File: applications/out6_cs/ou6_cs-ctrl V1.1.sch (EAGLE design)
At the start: 82 parts, among them P3 SE1.5, P4 SE1.5, P5 SE1.5, Q1 BCP52, T1 AX1500, T2 AX1500, T3 AX1500, T4 AX1500, T5 AX1500, T6 AX1500, U1 74LV4051D, U2 OPA365AIDBV, U3 OPA365AIDBV, U4 OPA365AIDBV

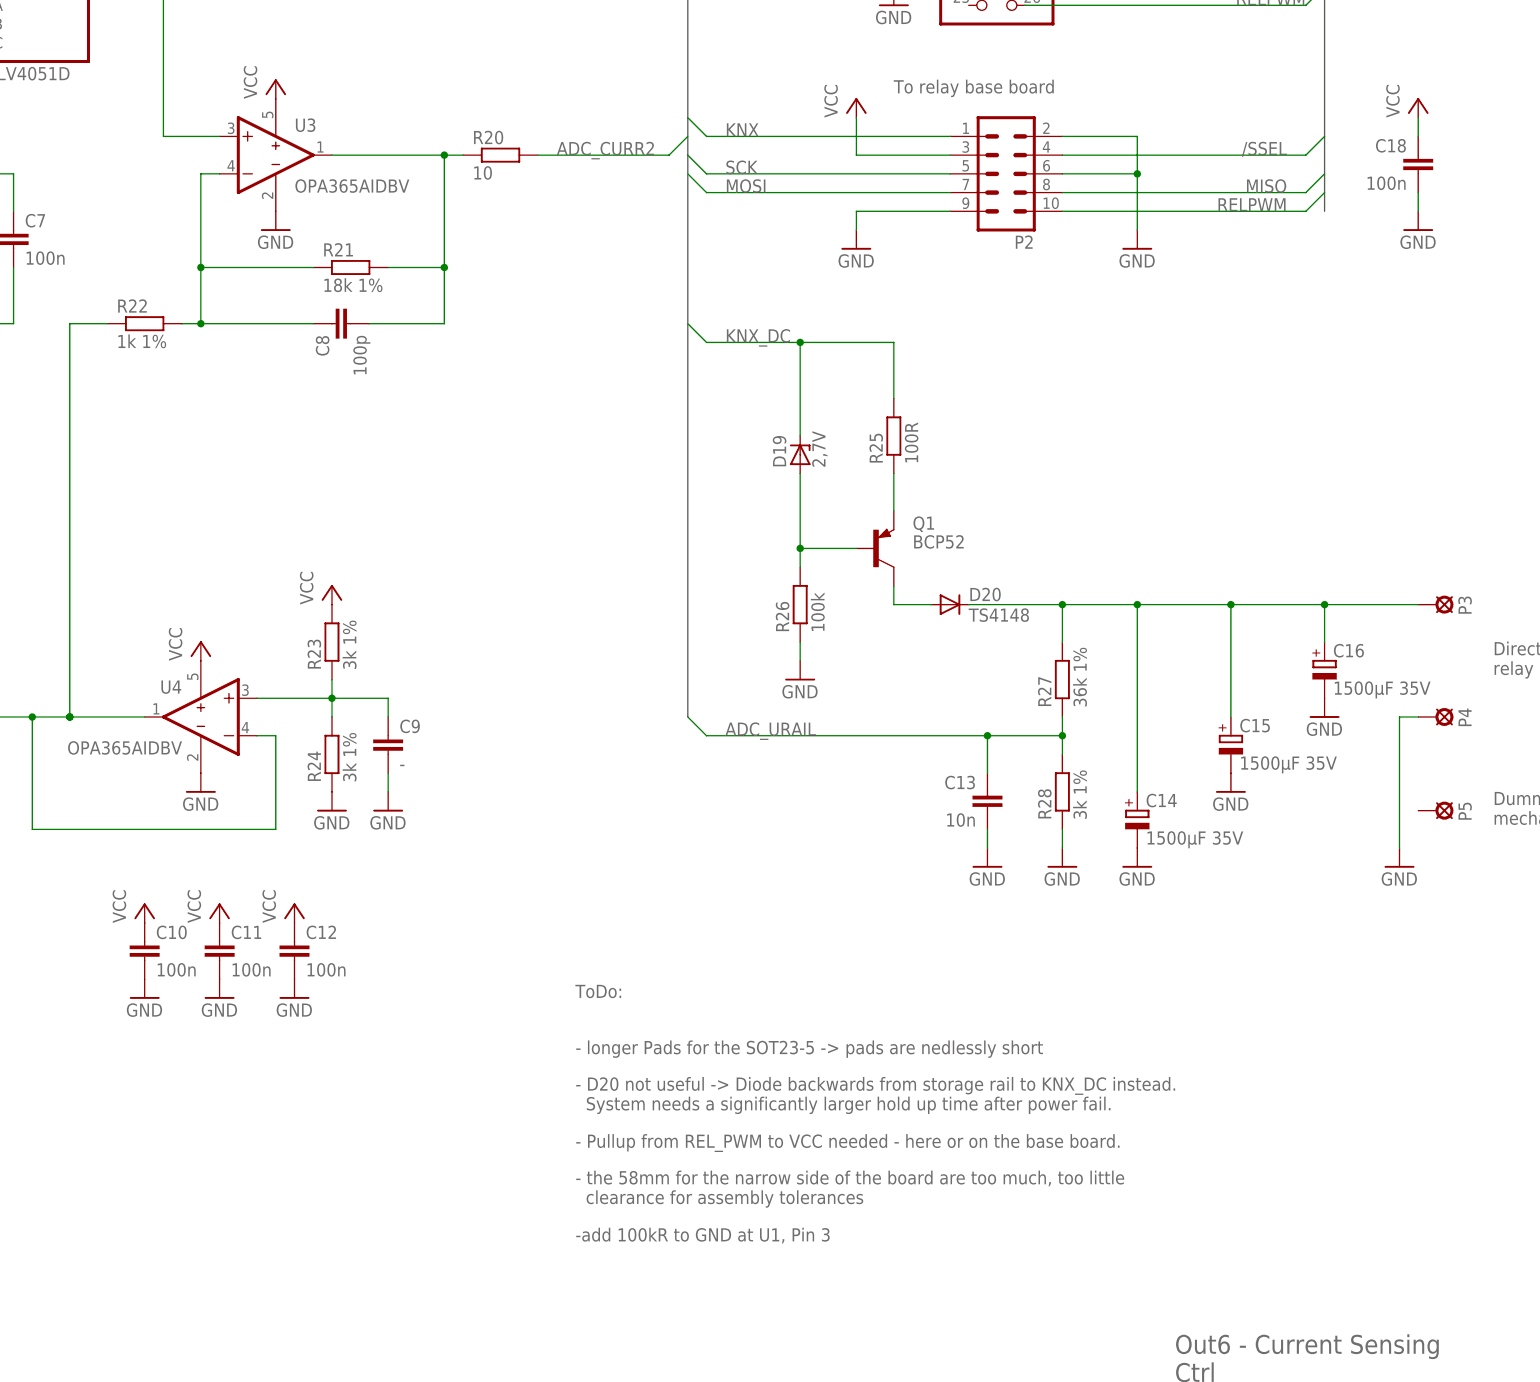
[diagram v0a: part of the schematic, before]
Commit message: Update App out6_cs, update Controller lpc1115_4te_top
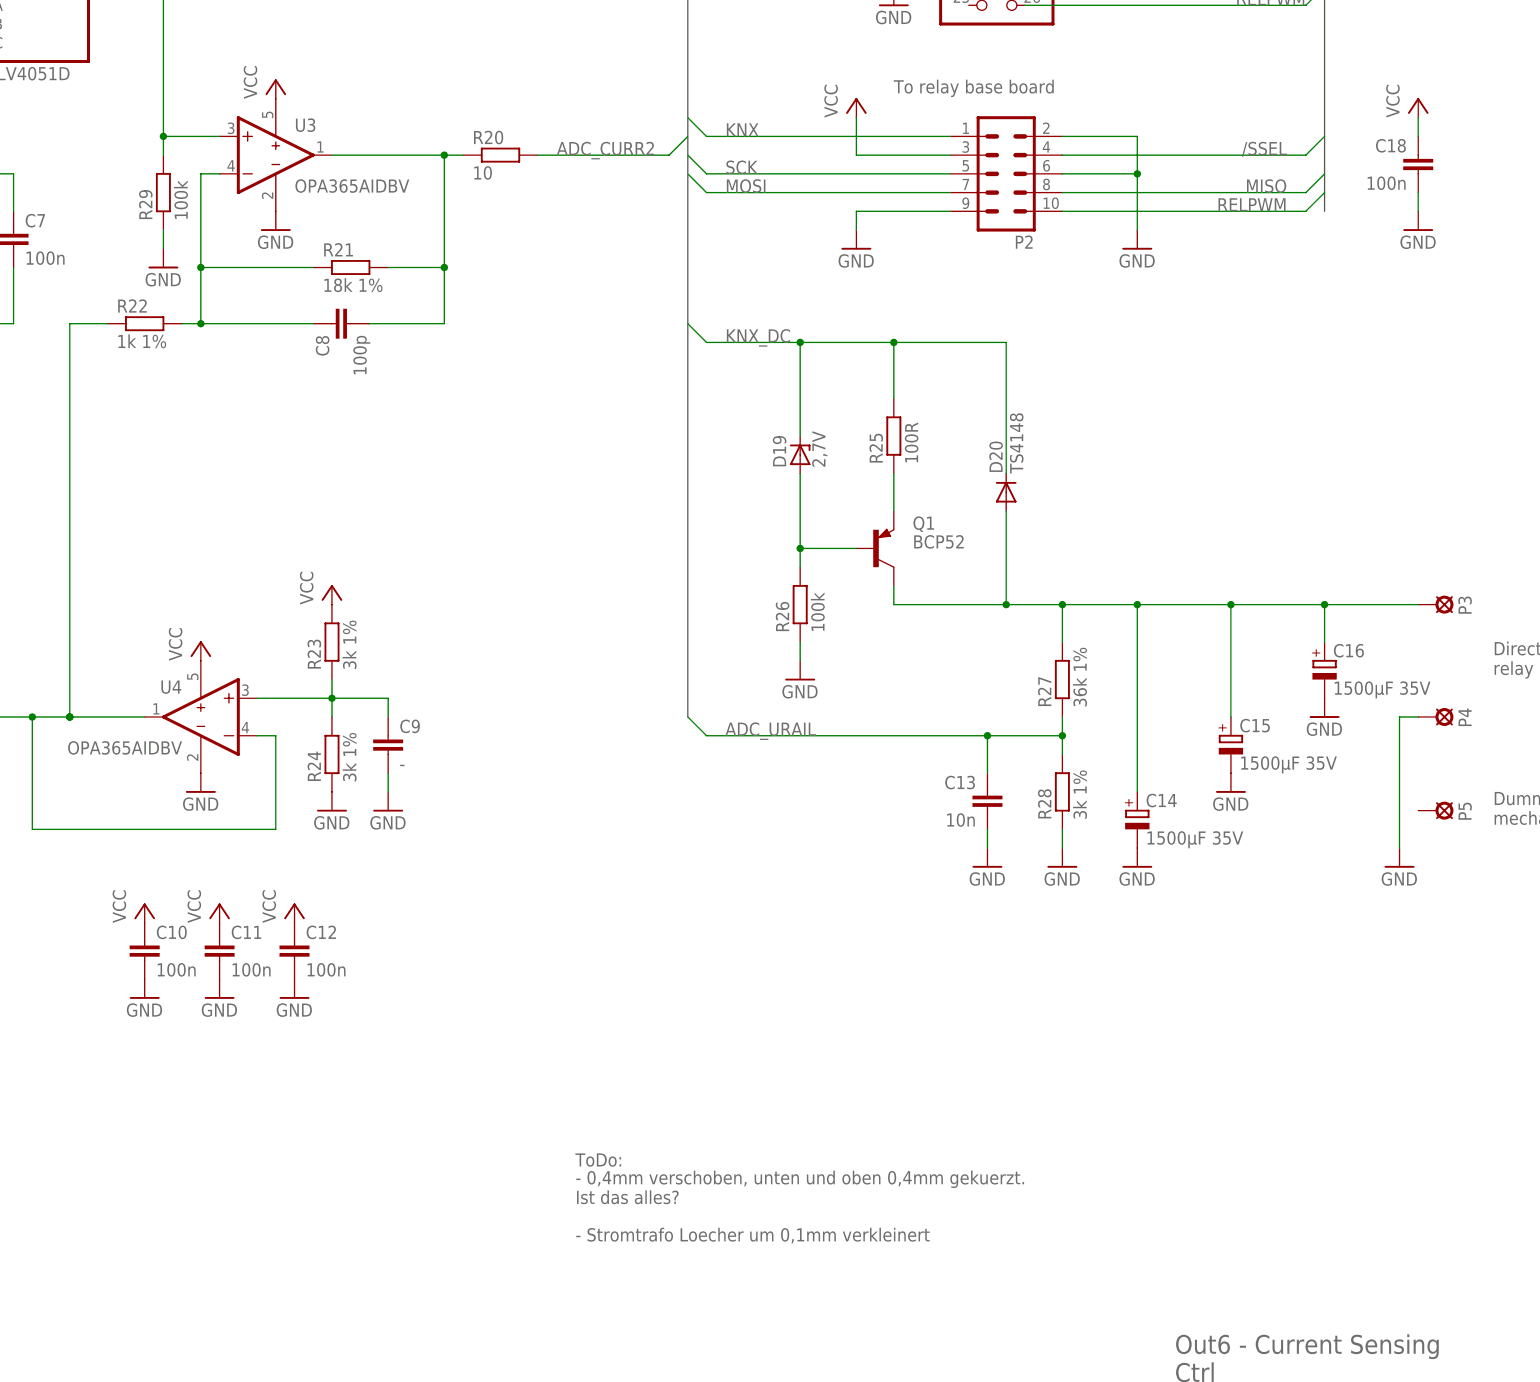
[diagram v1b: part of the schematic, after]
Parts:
- added R29: 100k, rcl:R-EU_R0805M
- D20: device diode:DIODE-MINIMELF -> diode:DIODE-D0805
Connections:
- removed net N$39: C14.+, C15.+, C16.+, D20.C, P3.MP, R27.2
- net GND: now also R29.1
- net KNX_DC: now also D20.C
- net N$16: now also R29.2
- net N$38: now also C14.+, C15.+, C16.+, P3.MP, R27.2
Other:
- note added: "- 0,4mm verschoben, unten und oben 0,4mm gekuerzt. Ist das alles?"
- note added: "- Stromtrafo Loecher um 0,1mm verkleinert"
- note removed: "- D20 not useful -> Diode backwards from storage rail to KNX_DC instead. System needs a significantly larger hold up time after power fail."
- note removed: "- Pullup from REL_PWM to VCC needed - here or on the base board."
- note removed: "- longer Pads for the SOT23-5 -> pads are nedlessly short"
- note removed: "- the 58mm for the narrow side of the board are too much, too little clearance for assembly tolerances"
- note removed: "-add 100kR to GND at U1, Pin 3"
- moved on the sheet: D20
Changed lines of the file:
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@@
 <part name="R26" library="rcl" deviceset="R-EU_" device="R0805M" value="100k"/>
 <part name="D19" library="diode" deviceset="ZENER-DIODE" device="SOT23" value="2,7V"/>
-<part name="D20" library="diode" deviceset="DIODE-" device="MINIMELF" value="TS4148"/>
+<part name="D20" library="diode" deviceset="DIODE-" device="D0805" value="TS4148"/>
 <part name="R27" library="rcl" deviceset="R-EU_" device="R0805M" value="36k 1%"/>
 <part name="R28" library="rcl" deviceset="R-EU_" device="R0805M" value="3k 1%"/>
@@
 <part name="P+11" library="supply1" deviceset="VCC" device=""/>
 <part name="P+12" library="supply1" deviceset="VCC" device=""/>
+<part name="R29" library="rcl" deviceset="R-EU_" device="R0805M" value="100k"/>
+<part name="GND24" library="supply1" deviceset="GND" device=""/>
 </parts>
 <sheets>
@@
 <text x="335.28" y="93.98" size="1.778" layer="95" align="top-left">Dummy connection only as
 mechanical support.</text>
-<text x="210.82" y="66.04" size="1.778" layer="95">ToDo:</text>
-<text x="210.82" y="58.42" size="1.778" layer="95">- longer Pads for the SOT23-5 -&gt; pads are nedlessly short</text>
-<text x="210.82" y="50.8" size="1.778" layer="95">- D20 not useful -&gt; Diode backwards from storage rail to KNX_DC instead.
-  System needs a significantly larger hold up time after power fail.</text>
-<text x="210.82" y="45.72" size="1.778" layer="95">- Pullup from REL_PWM to VCC needed - here or on the base board.</text>
-<text x="210.82" y="38.1" size="1.778" layer="95">- the 58mm for the narrow side of the board are too much, too little
-  clearance for assembly tolerances</text>
-<text x="210.82" y="33.02" size="1.778" layer="95">-add 100kR to GND at U1, Pin 3</text>
+<text x="210.82" y="43.18" size="1.778" layer="95">ToDo:</text>
+<text x="210.82" y="38.1" size="1.778" layer="95">- 0,4mm verschoben, unten und oben 0,4mm gekuerzt.
+Ist das alles?</text>
+<text x="210.82" y="33.02" size="1.778" layer="95">- Stromtrafo Loecher um 0,1mm verkleinert</text>
 </plain>
 <instances>
@@
 <instance part="R26" gate="G$1" x="241.3" y="119.38" rot="R90"/>
 <instance part="D19" gate="G$1" x="241.3" y="139.7" rot="R90"/>
-<instance part="D20" gate="G$1" x="261.62" y="119.38"/>
+<instance part="D20" gate="G$1" x="269.24" y="134.62" rot="R90"/>
 <instance part="R27" gate="G$1" x="276.86" y="109.22" rot="R90"/>
 <instance part="R28" gate="G$1" x="276.86" y="93.98" rot="R90"/>
@@
 <instance part="P+11" gate="VCC" x="325.12" y="187.96"/>
 <instance part="P+12" gate="VCC" x="325.12" y="226.06"/>
+<instance part="R29" gate="G$1" x="154.94" y="175.26" rot="R90"/>
+<instance part="GND24" gate="1" x="154.94" y="165.1"/>
 </instances>
 <busses>
@@
 <pinref part="GND23" gate="1" pin="GND"/>
 <wire x1="325.12" y1="210.82" x2="325.12" y2="213.36" width="0.1524" layer="91"/>
+</segment>
+<segment>
+<pinref part="R29" gate="G$1" pin="1"/>
+<pinref part="GND24" gate="1" pin="GND"/>
+<wire x1="154.94" y1="170.18" x2="154.94" y2="167.64" width="0.1524" layer="91"/>
 </segment>
 </net>
@@
 <wire x1="154.94" y1="226.06" x2="162.56" y2="226.06" width="0.1524" layer="91"/>
 <junction x="154.94" y="226.06"/>
+<pinref part="R29" gate="G$1" pin="2"/>
+<wire x1="154.94" y1="180.34" x2="154.94" y2="182.88" width="0.1524" layer="91"/>
+<junction x="154.94" y="182.88"/>
 </segment>
 </net>
@@
 <junction x="241.3" y="154.94"/>
 <label x="231.14" y="154.94" size="1.778" layer="95"/>
+<pinref part="D20" gate="G$1" pin="C"/>
+<wire x1="254" y1="154.94" x2="269.24" y2="154.94" width="0.1524" layer="91"/>
+<wire x1="269.24" y1="154.94" x2="269.24" y2="137.16" width="0.1524" layer="91"/>
+<junction x="254" y="154.94"/>
 </segment>
 </net>
@@
 <pinref part="Q1" gate="G$1" pin="C"/>
 <wire x1="254" y1="121.92" x2="254" y2="119.38" width="0.1524" layer="91"/>
-<pinref part="D20" gate="G$1" pin="A"/>
-<wire x1="254" y1="119.38" x2="259.08" y2="119.38" width="0.1524" layer="91"/>
-</segment>
-</net>
-<net name="N$39" class="0">
-<segment>
-<pinref part="D20" gate="G$1" pin="C"/>
-<wire x1="264.16" y1="119.38" x2="276.86" y2="119.38" width="0.1524" layer="91"/>
 <pinref part="R27" gate="G$1" pin="2"/>
 <wire x1="276.86" y1="119.38" x2="276.86" y2="114.3" width="0.1524" layer="91"/>
 <wire x1="276.86" y1="119.38" x2="287.02" y2="119.38" width="0.1524" layer="91"/>
-<junction x="276.86" y="119.38"/>
 <pinref part="P3" gate="1" pin="MP"/>
 <pinref part="C14" gate="G$1" pin="+"/>
@@
 <wire x1="312.42" y1="114.3" x2="312.42" y2="119.38" width="0.1524" layer="91"/>
 <junction x="312.42" y="119.38"/>
-</segment>
-</net>
+<wire x1="254" y1="119.38" x2="269.24" y2="119.38" width="0.1524" layer="91"/>
+<junction x="276.86" y="119.38"/>
+<pinref part="D20" gate="G$1" pin="A"/>
+<wire x1="269.24" y1="119.38" x2="276.86" y2="119.38" width="0.1524" layer="91"/>
+<wire x1="269.24" y1="132.08" x2="269.24" y2="119.38" width="0.1524" layer="91"/>
+<junction x="269.24" y="119.38"/>
+</segment>
+</net>

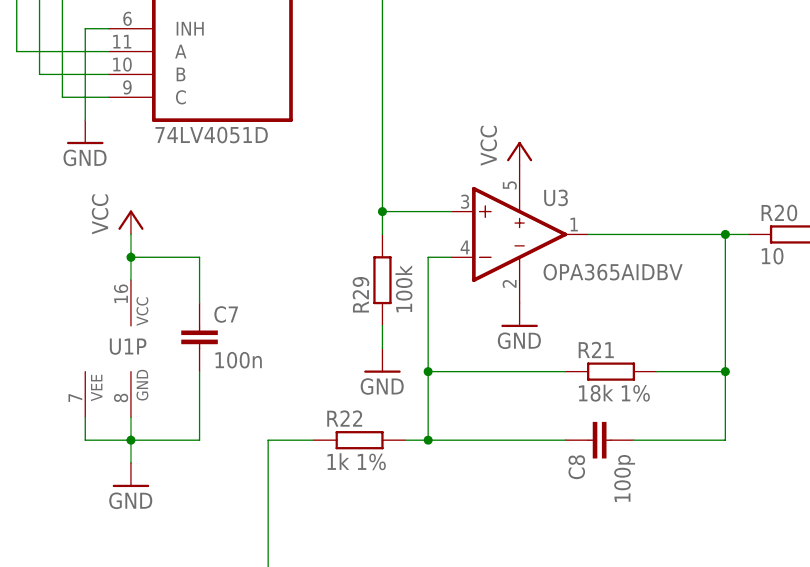
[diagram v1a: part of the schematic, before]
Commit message: R29 auf out6_cs-ctrl V1.1 auf unbestückt geändert
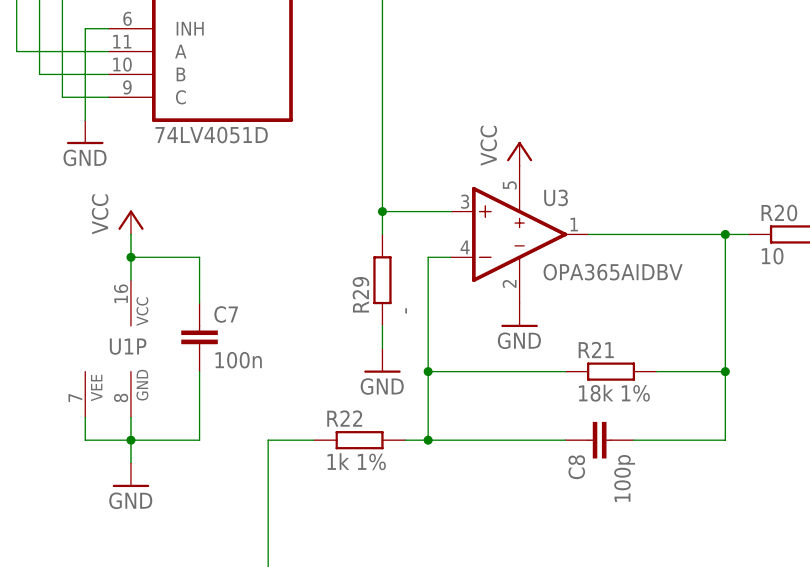
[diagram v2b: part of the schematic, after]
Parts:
- R29: value 100k -> -
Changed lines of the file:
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@@
 <part name="P+11" library="supply1" deviceset="VCC" device=""/>
 <part name="P+12" library="supply1" deviceset="VCC" device=""/>
-<part name="R29" library="rcl" deviceset="R-EU_" device="R0805M" value="100k"/>
+<part name="R29" library="rcl" deviceset="R-EU_" device="R0805M" value="-"/>
 <part name="GND24" library="supply1" deviceset="GND" device=""/>
 </parts>
